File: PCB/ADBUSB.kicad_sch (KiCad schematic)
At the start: 5 parts, among them J1 MLD-MDC-4-02, J2 MLD-MDC-4-02, SW1 SW_Slide_DPDT SHOU HAN MSK-22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, U1 ProMicro

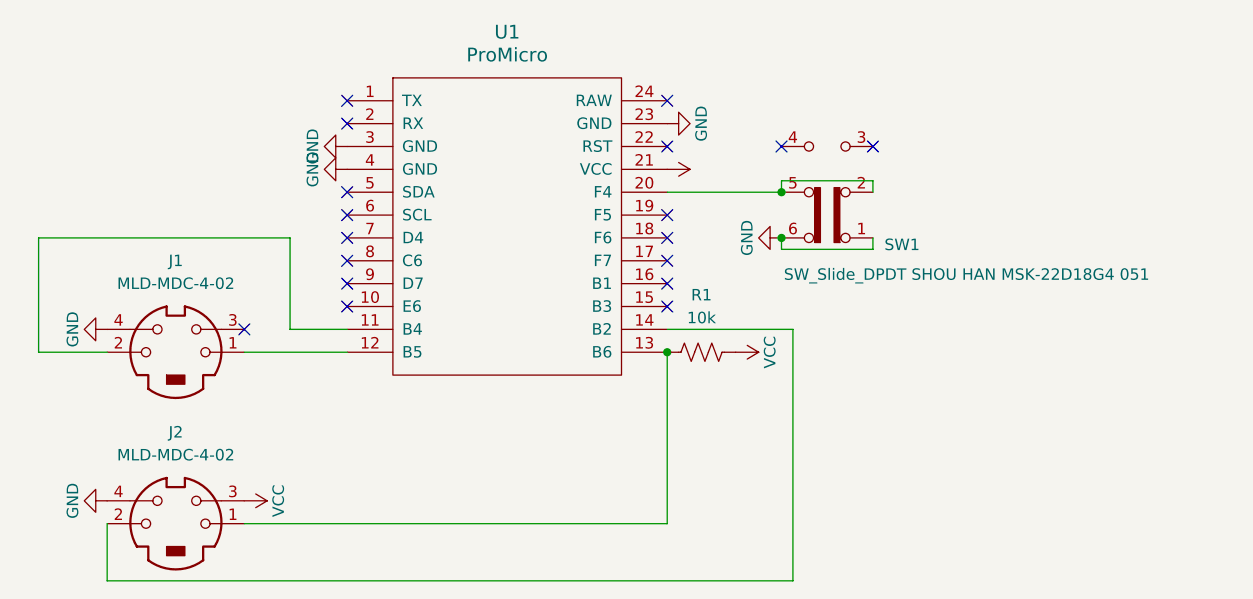
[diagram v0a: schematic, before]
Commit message: Update for diode, pushbutton, raw
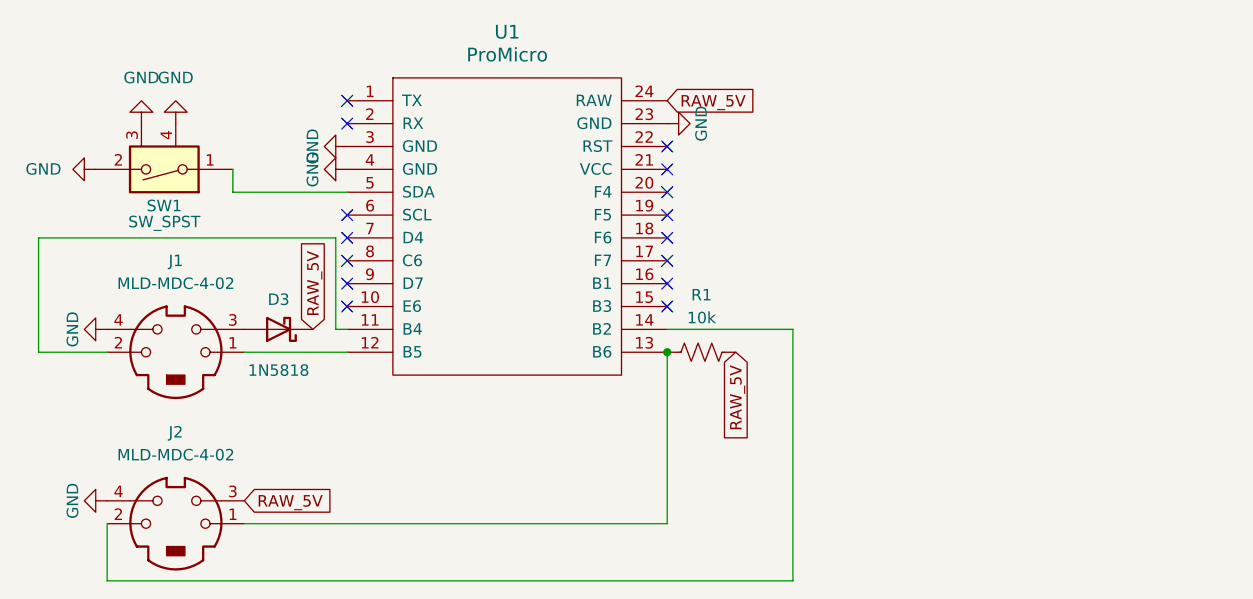
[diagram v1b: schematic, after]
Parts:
- removed SW1: SW_Slide_DPDT SHOU HAN MSK-22D18G4 051, DIN5:DPDT slide switch C7507433, symbol Switch:SW_Slide_DPDT
- added D3: 1N5818, Diode_THT:D_DO-41_SOD81_P7.62mm_Horizontal, symbol Diode:1N5818
- added SW1: SW_SPST, Pushbutton:SPST_power_switch_horizontal, symbol Switch:SW_DIP_x01
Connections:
- net GND: now also SW1.2, SW1.3, SW1.4 (3)
- net RAW_5V: now reaches U1.24 (RAW)
- net RAW_5V: now also J2.3, R1.2, D3.1 (K)
- net at U1.5 (SDA): now also SW1.1
- net at J1.3: now also D3.2 (A)
- removed net VCC: J2.3, R1.2, U1.21 (VCC)
- no-connect marks 18 -> 15
